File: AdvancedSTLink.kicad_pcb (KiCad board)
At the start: 4 copper layers, 49.9 x 15 mm, 54 parts, among them J1 USB_C_Receptacle, J2 Conn_02x03_Odd_Even, J3 Conn_01x06, J4 Conn_02x03_Odd_Even, SW1 SW_SPDT, U1 STM32F205RETx, U2 XC6206P332MR, U3 USBLC6-2P6, U4 MP2359, U5 USBLC6-2P6, U6 USBLC6-2P6, Y1 X322512MSB4SI

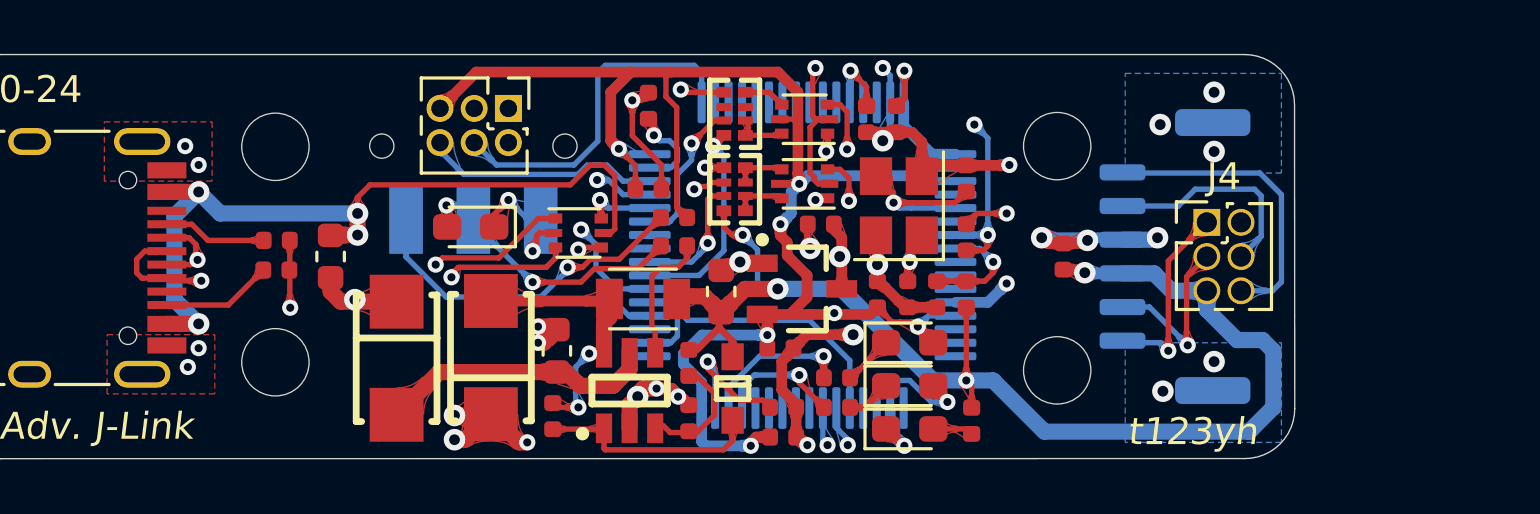
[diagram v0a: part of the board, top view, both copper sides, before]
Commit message: Rearrange RST.
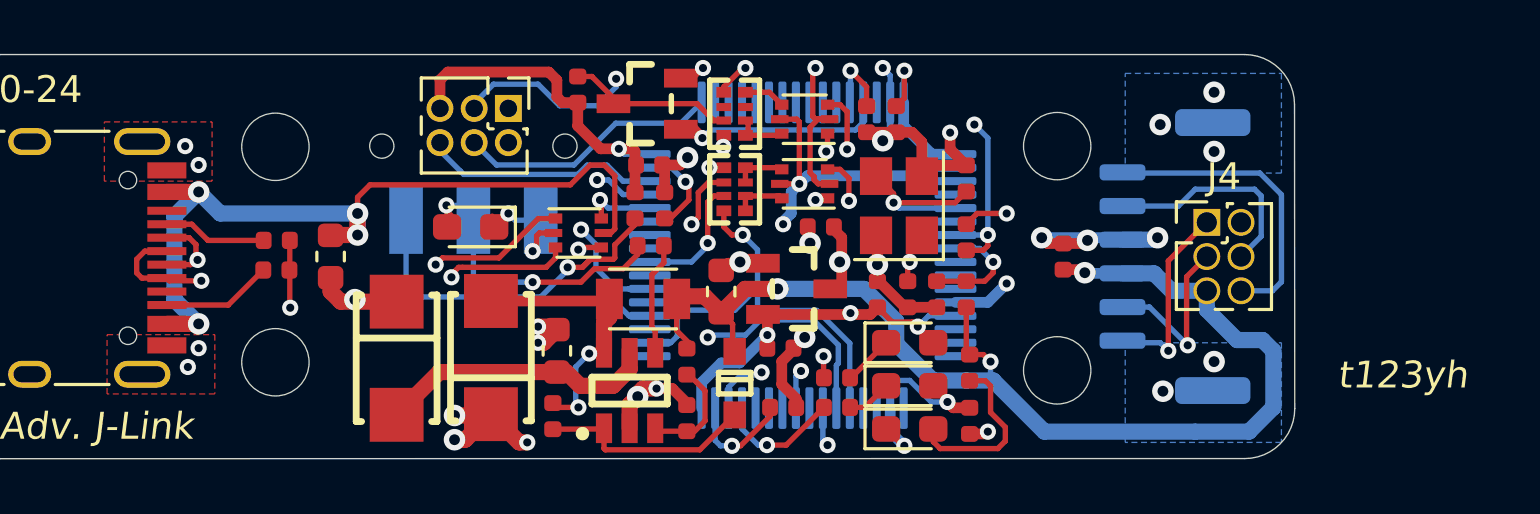
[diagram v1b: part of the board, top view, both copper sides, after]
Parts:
- added Q1: S8050, lc:SOT-23(SOT-23-3), F.Cu at (188.1, 98.8)
- added R6: 10k, Resistor_SMD:R_0402_1005Metric, F.Cu at (185.5, 98.3)
- RN1, RN2: value 220×4 -> 100×4
- U2: footprint lc:SOT-23-3L -> lc:SOT-23(SOT-23-3)
- moved C11 6.95 mm to (200.0, 110.6), turned to 270 degrees
- moved C14 3.75 mm to (188.7, 102.6)
- moved R16 1.98 mm to (200.0, 108.6)
- moved R9 1.52 mm to (187.6, 102.6), turned to 270 degrees
- moved C9 0.90 mm to (188.1, 101.1)
- moved R1 0.87 mm to (188.2, 104.1)
- moved D4 0.21 mm to (191.3, 109.2)
- moved U2 0.20 mm to (193.6, 105.7)
- moved C4 0.10 mm to (194.5, 103.4)
- moved R14 0.09 mm to (189.5, 108.4)
- moved R15 0.07 mm to (189.5, 110.5)
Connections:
- RN2 pad 7: RST2 -> Net-(Q1-Pad3)
- RN2 pad 8: RST1 -> RST_SENSE
- U1 pad 25: Net-(U1-Pad25) -> RST_SENSE
- U1 pad 39: RST1 -> Net-(U1-Pad39)
- U1 pad 61: Net-(U1-Pad61) -> RST_PULL
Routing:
- net RST_SENSE: track 0.00 -> 11.8 mm, vias 0 -> 2
- net +3V3: track 78.6 -> 69.1 mm, vias 9 -> 8
- net RST_PULL: track 0.00 -> 7.89 mm, vias 0 -> 1
- net RST1: track 7.74 -> 0.00 mm, vias 1 -> 0
- net Net-(Q1-Pad3): track 0.00 -> 6.68 mm
- net RST2: track 6.30 -> 0.78 mm, vias 1 -> 0
- net Net-(D5-Pad2): track 1.50 -> 6.63 mm
- net GND: track 65.7 -> 61.1 mm
- net TDO: track 17.8 -> 21.9 mm
- net STM_SWCLK: track 13.0 -> 9.75 mm
- net LED2: track 5.58 -> 7.08 mm, vias 1 -> 2
- net TMS2: track 14.8 -> 15.9 mm
- net Net-(FB1-Pad2): track 29.3 -> 30.1 mm
- net Net-(C14-Pad1): track 3.36 -> 4.16 mm
- net Net-(R1-Pad1): track 4.94 -> 4.21 mm
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
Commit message: 拼板
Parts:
- added C1: 33pF, Capacitor_SMD:C_0402_1005Metric, F.Cu at (176.6, 86.1)
- added C10: 100nF, Capacitor_SMD:C_0402_1005Metric, F.Cu at (177.7, 86.1)
- added C11: 100nF, Capacitor_SMD:C_0402_1005Metric, F.Cu at (174.3, 81.4)
- added C12: 22uF, Capacitor_SMD:C_0603_1608Metric, F.Cu at (183.5, 86.2)
- added C13: 2.2uF, Capacitor_SMD:C_0402_1005Metric, F.Cu at (181.2, 81.9)
- added C14: 2.2uF, Capacitor_SMD:C_0402_1005Metric, F.Cu at (185.6, 89.4)
- added C15: 100nF, Capacitor_SMD:C_0402_1005Metric, F.Cu at (170.8, 87.5)
- added C2: 33pF, Capacitor_SMD:C_0402_1005Metric, F.Cu at (174.4, 90.4)
- added C3: 100nF, Capacitor_SMD:C_0402_1005Metric, F.Cu at (174.4, 88.2)
- added C4: 2.2uF, Capacitor_SMD:C_0402_1005Metric, F.Cu at (179.8, 88.6)
- added C5: 2.2uF, Capacitor_SMD:C_0402_1005Metric, F.Cu at (181.3, 84.1)
- added C6: 10uF, Capacitor_SMD:C_0603_1608Metric, F.Cu at (189.6, 84.0)
- added C7: 100nF, Capacitor_SMD:C_0402_1005Metric, F.Cu at (189.7, 81.6)
- added C8: 100nF, Capacitor_SMD:C_0402_1005Metric, F.Cu at (177.0, 92.6)
- added C9: 100nF, Capacitor_SMD:C_0402_1005Metric, F.Cu at (186.2, 90.9)
- added D1: LED_Red, LED_SMD:LED_0603_1608Metric_Pad1.05x0.95mm_HandSolder, F.Cu at (176.5, 82.7)
- added D2: LED_Yellow, LED_SMD:LED_0603_1608Metric_Pad1.05x0.95mm_HandSolder, F.Cu at (176.5, 84.3)
- added D3: SS34, lc:SMA(DO-214AC)_S1, F.Cu at (192.0, 83.8)
- added D4: 1N4148W, lc:SOD-323, F.Cu at (183.0, 82.8)
- added D5: LED_Blue, LED_SMD:LED_0603_1608Metric_Pad1.05x0.95mm_HandSolder, F.Cu at (176.5, 81.1)
- added D6: LED_Blue, LED_SMD:LED_0603_1608Metric_Pad1.05x0.95mm_HandSolder, F.Cu at (192.8, 88.6)
- added D7: SS34, lc:SMA(DO-214AC)_S1, F.Cu at (195.5, 83.7)
- added FB1: Ferrite_Bead_Small, Inductor_SMD:L_0603_1608Metric, F.Cu at (198.0, 87.5)
- added H1: MountingHole, MountingHole:MountingHole_2.5mm, F.Cu at (171.0, 91.6)
- added H2: MountingHole, MountingHole:MountingHole_2.5mm, F.Cu at (171.0, 83.3)
- added H3: MountingHole, MountingHole:MountingHole_2.5mm, F.Cu at (200.0, 91.6)
- added H4: MountingHole, MountingHole:MountingHole_2.5mm, F.Cu at (200.0, 83.6)
- added J1: USB_C_Receptacle, Connector_USB:USB_C_Receptacle_HRO_TYPE-C-31-M-12, F.Cu at (208.1, 87.5)
- added J2: Conn_02x03_Odd_Even, Connector_PinHeader_1.27mm:PinHeader_2x03_P1.27mm_Vertical, F.Cu at (191.4, 93.0)
- added J3: Conn_01x06, Connector_Molex:Molex_CLIK-Mate_502382-0670_1x06-1MP_P1.25mm_Vertical, B.Cu at (166.6, 87.5)
- added J4: Conn_02x03_Odd_Even, Connector_PinHeader_1.27mm:PinHeader_2x03_P1.27mm_Vertical, F.Cu at (165.4, 88.8)
- added L1: DFE252010P-4R7M, Inductor_SMD:L_TDK_NLV25_2.5x2.0mm, F.Cu at (186.4, 85.9)
- added Q1: S8050, lc:SOT-23(SOT-23-3), F.Cu at (186.2, 93.2)
- added R1: 39k, Resistor_SMD:R_0402_1005Metric, F.Cu at (186.1, 87.9)
- added R14: 120k, Resistor_SMD:R_0402_1005Metric, F.Cu at (184.8, 83.6)
- added R15: 39k, Resistor_SMD:R_0402_1005Metric, F.Cu at (184.8, 81.5)
- added R16: 1.8k, Resistor_SMD:R_0402_1005Metric, F.Cu at (174.3, 83.4)
- added R17: 100k, Resistor_SMD:R_0402_1005Metric, F.Cu at (178.1, 92.6)
- added R2: 10k, Resistor_SMD:R_0402_1005Metric, F.Cu at (175.5, 86.1)
- added R3: 10k, Resistor_SMD:R_0402_1005Metric, F.Cu at (174.4, 86.1)
- added R4: 5.1k, Resistor_SMD:R_0402_1005Metric, F.Cu at (200.0, 88.1)
- added R5: 5.1k, Resistor_SMD:R_0402_1005Metric, F.Cu at (200.0, 87.0)
- added R6: 10k, Resistor_SMD:R_0402_1005Metric, F.Cu at (188.8, 93.7)
- added R7: 2.2k, Resistor_SMD:R_0402_1005Metric, F.Cu at (179.2, 81.9)
- added R8: 2.2k, Resistor_SMD:R_0402_1005Metric, F.Cu at (179.2, 83.0)
- added R9: 2.2k, Resistor_SMD:R_0402_1005Metric, F.Cu at (186.7, 89.4)
- added RN1: 100×4, lc:0402_RX4, F.Cu at (183.0, 90.0)
- added RN2: 100×4, lc:0402_RX4, F.Cu at (183.0, 92.8)
- added SW1: SW_SPDT, Button_Switch_SMD:SW_SPDT_CK-JS102011SAQN, B.Cu at (192.7, 91.6)
- added U1: STM32F205RETx, Package_QFP:LQFP-64_10x10mm_P0.5mm, B.Cu at (180.5, 87.5)
- added U2: XC6206P332MR, lc:SOT-23(SOT-23-3), F.Cu at (180.7, 86.3)
- added U3: USBLC6-2P6, Package_TO_SOT_SMD:SOT-666, F.Cu at (188.8, 88.4)
- added U4: MP2359, lc:SOT-23-6, F.Cu at (186.9, 82.5)
- added U5: USBLC6-2P6, Package_TO_SOT_SMD:SOT-666, F.Cu at (180.4, 92.6)
- added U6: USBLC6-2P6, Package_TO_SOT_SMD:SOT-666, F.Cu at (180.4, 90.2)
- added Y1: X322512MSB4SI, Crystal:Crystal_SMD_3225-4Pin_3.2x2.5mm, F.Cu at (176.9, 89.4)
- added mouse-bite-3mm-slot: VAL**, mouse_bite:mouse-bite-3mm-slot, F.Cu at (170.0, 96.0)
- added mouse-bite-3mm-slot: VAL**, mouse_bite:mouse-bite-3mm-slot, F.Cu at (204.3, 96.0)
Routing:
- net (no net): track 0.00 -> 665.8 mm, vias 0 -> 94
- added copper zone on B.Cu, net (none)
- added copper zone on F.Cu, net (none)
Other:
- board size 49.9 x 15 mm -> 49.9 x 32 mm

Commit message: fabrication version
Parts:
- FB1 (x2): footprint Inductor_SMD:L_0603_1608Metric -> Inductor_SMD:L_0805_2012Metric
- moved FB1 1.95 mm to (196.2, 88.4), turned to 0 degrees
- moved FB1 1.95 mm to (178.0, 103.6), turned to 180 degrees
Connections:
- C1 pad 1: (no net) -> Net-(C1-Pad1)
- C1 pad 2: (no net) -> GND
- C10 pad 1: (no net) -> +3V3
- C10 pad 2: (no net) -> GND
- C11 pad 1: (no net) -> +3V3
- C11 pad 2: (no net) -> GND
- C12 pad 1: (no net) -> V_OUT_3.3
- C12 pad 2: (no net) -> GND
- C13 pad 1: (no net) -> GND
- C13 pad 2: (no net) -> Net-(C13-Pad2)
- C14 pad 1: (no net) -> Net-(C14-Pad1)
- C14 pad 2: (no net) -> GND
- C15 pad 1: (no net) -> V_OUT_3.3
- C15 pad 2: (no net) -> GND
- C2 pad 1: (no net) -> GND
- C2 pad 2: (no net) -> Net-(C2-Pad2)
- C3 pad 1: (no net) -> GND
- C3 pad 2: (no net) -> STM_NRST
- C4 pad 1: (no net) -> VBUS
- C4 pad 2: (no net) -> GND
- C5 pad 1: (no net) -> +3V3
- C5 pad 2: (no net) -> GND
- C6 pad 1: (no net) -> Net-(C6-Pad1)
- C6 pad 2: (no net) -> GND
- C7 pad 1: (no net) -> Net-(C7-Pad1)
- C7 pad 2: (no net) -> Net-(C7-Pad2)
- C8 pad 1: (no net) -> +3V3
- C8 pad 2: (no net) -> GND
- C9 pad 1: (no net) -> +3V3
- C9 pad 2: (no net) -> GND
- D1 pad 1: (no net) -> Net-(D1-Pad1)
- D1 pad 2: (no net) -> +3V3
- D2 pad 1: (no net) -> Net-(D2-Pad1)
- D2 pad 2: (no net) -> +3V3
- D3 pad 1: (no net) -> Net-(C7-Pad2)
- D3 pad 2: (no net) -> GND
- D4 pad 1: (no net) -> Net-(C7-Pad1)
- D4 pad 2: (no net) -> V_OUT_3.3
- D5 pad 1: (no net) -> GND
- D5 pad 2: (no net) -> Net-(D5-Pad2)
- D6 pad 1: (no net) -> GND
- D6 pad 2: (no net) -> Net-(D6-Pad2)
- D7 pad 1: (no net) -> Net-(C6-Pad1)
- D7 pad 2: (no net) -> VBUS
- FB1 pad 1: (no net) -> VBUS
- FB1 pad 2: (no net) -> Net-(FB1-Pad2)
- J1 pad A1: (no net) -> GND
- J1 pad A12: (no net) -> GND
- J1 pad A4: (no net) -> Net-(FB1-Pad2)
- J1 pad A5: (no net) -> Net-(J1-PadA5)
- J1 pad A6: (no net) -> USB_IN_DP
- J1 pad A7: (no net) -> USB_IN_DN
- J1 pad A8: (no net) -> Net-(J1-PadA8)
- J1 pad A9: (no net) -> Net-(FB1-Pad2)
- J1 pad B1: (no net) -> GND
- J1 pad B12: (no net) -> GND
- J1 pad B4: (no net) -> Net-(FB1-Pad2)
- J1 pad B5: (no net) -> Net-(J1-PadB5)
- J1 pad B6: (no net) -> USB_IN_DP
- J1 pad B7: (no net) -> USB_IN_DN
- J1 pad B8: (no net) -> Net-(J1-PadB8)
- J1 pad B9: (no net) -> Net-(FB1-Pad2)
- J1 pad S1: (no net) -> GND
- J2 pad 1: (no net) -> Net-(J2-Pad1)
- J2 pad 2: (no net) -> GND
- J2 pad 3: (no net) -> STM_NRST
- J2 pad 4: (no net) -> STM_SWCLK
- J2 pad 5: (no net) -> +3V3
- J2 pad 6: (no net) -> STM_SWDIO
- J3 pad 1: (no net) -> T_SWO_O
- J3 pad 2: (no net) -> T_NRST_O
- J3 pad 3: (no net) -> V_OUT_3.3
- J3 pad 4: (no net) -> GND
- J3 pad 5: (no net) -> T_SWCLK_O
- J3 pad 6: (no net) -> T_SWDIO_O
- J3 pad MP: (no net) -> GND
- J4 pad 1: (no net) -> T_SWO_O
- J4 pad 2: (no net) -> GND
- J4 pad 3: (no net) -> T_NRST_O
- J4 pad 4: (no net) -> T_SWCLK_O
- J4 pad 5: (no net) -> V_OUT_3.3
- J4 pad 6: (no net) -> T_SWDIO_O
- L1 pad 1: (no net) -> Net-(C7-Pad2)
- L1 pad 2: (no net) -> V_OUT_3.3
- Q1 pad 1: (no net) -> RST_PULL
- Q1 pad 2: (no net) -> GND
- Q1 pad 3: (no net) -> Net-(Q1-Pad3)
- R1 pad 1: (no net) -> Net-(R1-Pad1)
- R1 pad 2: (no net) -> Net-(D6-Pad2)
- R14 pad 1: (no net) -> Net-(R14-Pad1)
- R14 pad 2: (no net) -> V_OUT_3.3
- R15 pad 1: (no net) -> GND
- R15 pad 2: (no net) -> Net-(R14-Pad1)
- R16 pad 1: (no net) -> Net-(D5-Pad2)
- R16 pad 2: (no net) -> V_OUT_3.3
- R17 pad 1: (no net) -> Net-(R17-Pad1)
- R17 pad 2: (no net) -> GND
- R2 pad 1: (no net) -> GND
- R2 pad 2: (no net) -> Net-(R2-Pad2)
- R3 pad 1: (no net) -> V_OUT_3.3
- R3 pad 2: (no net) -> Net-(R2-Pad2)
- R4 pad 1: (no net) -> GND
- R4 pad 2: (no net) -> Net-(J1-PadA5)
- R5 pad 1: (no net) -> GND
- R5 pad 2: (no net) -> Net-(J1-PadB5)
- R6 pad 1: (no net) -> Net-(Q1-Pad3)
- R6 pad 2: (no net) -> +3V3
- R7 pad 1: (no net) -> Net-(D1-Pad1)
- R7 pad 2: (no net) -> LED1
- R8 pad 1: (no net) -> Net-(D2-Pad1)
- R8 pad 2: (no net) -> LED2
- R9 pad 1: (no net) -> +3V3
- R9 pad 2: (no net) -> Net-(R9-Pad2)
- RN1 pad 1: (no net) -> T_SWCLK_I
- RN1 pad 2: (no net) -> T_SWCLK_I
- RN1 pad 3: (no net) -> T_SWDIO_I
- RN1 pad 4: (no net) -> T_SWDIO_I
- RN1 pad 5: (no net) -> TMS1
- RN1 pad 6: (no net) -> TMS2
- RN1 pad 7: (no net) -> TCK2
- RN1 pad 8: (no net) -> TCK1
- RN2 pad 1: (no net) -> T_NRST_I
- RN2 pad 2: (no net) -> T_NRST_I
- RN2 pad 3: (no net) -> Net-(RN2-Pad3)
- RN2 pad 4: (no net) -> T_SWO_I
- RN2 pad 5: (no net) -> TDO
- RN2 pad 6: (no net) -> Net-(RN2-Pad6)
- RN2 pad 7: (no net) -> Net-(Q1-Pad3)
- RN2 pad 8: (no net) -> RST_SENSE
- SW1 pad 1: (no net) -> Net-(R9-Pad2)
- SW1 pad 2: (no net) -> Net-(D6-Pad2)
- SW1 pad 3: (no net) -> GND
- U1 pad 1: (no net) -> +3V3
- U1 pad 10: (no net) -> Net-(U1-Pad10)
- U1 pad 11: (no net) -> Net-(U1-Pad11)
- U1 pad 12: (no net) -> GND
- U1 pad 13: (no net) -> +3V3
- U1 pad 14: (no net) -> Net-(U1-Pad14)
- U1 pad 15: (no net) -> Net-(U1-Pad15)
- U1 pad 16: (no net) -> Net-(U1-Pad16)
- U1 pad 17: (no net) -> Net-(U1-Pad17)
- U1 pad 18: (no net) -> GND
- U1 pad 19: (no net) -> +3V3
- U1 pad 2: (no net) -> Net-(U1-Pad2)
- U1 pad 20: (no net) -> Net-(U1-Pad20)
- U1 pad 21: (no net) -> TCK1
- U1 pad 22: (no net) -> TMS1
- U1 pad 23: (no net) -> TMS2
- U1 pad 24: (no net) -> Net-(U1-Pad24)
- U1 pad 25: (no net) -> RST_SENSE
- U1 pad 26: (no net) -> Net-(U1-Pad26)
- U1 pad 27: (no net) -> Net-(U1-Pad27)
- U1 pad 28: (no net) -> Net-(U1-Pad28)
- U1 pad 29: (no net) -> LED1
- U1 pad 3: (no net) -> Net-(U1-Pad3)
- U1 pad 30: (no net) -> LED2
- U1 pad 31: (no net) -> Net-(C13-Pad2)
- U1 pad 32: (no net) -> +3V3
- U1 pad 33: (no net) -> Net-(U1-Pad33)
- U1 pad 34: (no net) -> TCK1
- U1 pad 35: (no net) -> Net-(U1-Pad35)
- U1 pad 36: (no net) -> TDO
- U1 pad 37: (no net) -> TCK1
- U1 pad 38: (no net) -> TDO
- U1 pad 39: (no net) -> Net-(U1-Pad39)
- U1 pad 4: (no net) -> Net-(U1-Pad4)
- U1 pad 40: (no net) -> TCK2
- U1 pad 41: (no net) -> Net-(U1-Pad41)
- U1 pad 42: (no net) -> Net-(U1-Pad42)
- U1 pad 43: (no net) -> RST2
- U1 pad 44: (no net) -> USB_DN
- U1 pad 45: (no net) -> USB_DP
- U1 pad 46: (no net) -> STM_SWDIO
- U1 pad 47: (no net) -> Net-(C14-Pad1)
- U1 pad 48: (no net) -> +3V3
- U1 pad 49: (no net) -> STM_SWCLK
- U1 pad 5: (no net) -> Net-(C2-Pad2)
- U1 pad 50: (no net) -> Net-(U1-Pad50)
- U1 pad 51: (no net) -> Net-(U1-Pad51)
- U1 pad 52: (no net) -> Net-(U1-Pad52)
- U1 pad 53: (no net) -> Net-(U1-Pad53)
- U1 pad 54: (no net) -> Net-(U1-Pad54)
- U1 pad 55: (no net) -> Net-(U1-Pad55)
- U1 pad 56: (no net) -> Net-(U1-Pad56)
- U1 pad 57: (no net) -> Net-(U1-Pad57)
- U1 pad 58: (no net) -> Net-(U1-Pad58)
- U1 pad 59: (no net) -> Net-(U1-Pad59)
- U1 pad 6: (no net) -> Net-(C1-Pad1)
- U1 pad 60: (no net) -> Net-(R17-Pad1)
- U1 pad 61: (no net) -> RST_PULL
- U1 pad 62: (no net) -> Net-(U1-Pad62)
- U1 pad 63: (no net) -> GND
- U1 pad 64: (no net) -> +3V3
- U1 pad 7: (no net) -> STM_NRST
- U1 pad 8: (no net) -> Net-(R2-Pad2)
- U1 pad 9: (no net) -> Net-(U1-Pad9)
- U2 pad 1: (no net) -> GND
- U2 pad 2: (no net) -> +3V3
- U2 pad 3: (no net) -> VBUS
- U3 pad 1: (no net) -> USB_IN_DN
- U3 pad 2: (no net) -> GND
- U3 pad 3: (no net) -> USB_IN_DP
- U3 pad 4: (no net) -> USB_DP
- U3 pad 5: (no net) -> Net-(FB1-Pad2)
- U3 pad 6: (no net) -> USB_DN
- U4 pad 1: (no net) -> Net-(C7-Pad1)
- U4 pad 2: (no net) -> GND
- U4 pad 3: (no net) -> Net-(R14-Pad1)
- U4 pad 4: (no net) -> Net-(R1-Pad1)
- U4 pad 5: (no net) -> Net-(C6-Pad1)
- U4 pad 6: (no net) -> Net-(C7-Pad2)
- U5 pad 1: (no net) -> T_NRST_O
- U5 pad 2: (no net) -> GND
- U5 pad 3: (no net) -> T_SWO_O
- U5 pad 4: (no net) -> T_SWO_I
- U5 pad 5: (no net) -> +3V3
- U5 pad 6: (no net) -> T_NRST_I
- U6 pad 1: (no net) -> T_SWCLK_O
- U6 pad 2: (no net) -> GND
- U6 pad 3: (no net) -> T_SWDIO_O
- U6 pad 4: (no net) -> T_SWDIO_I
- U6 pad 5: (no net) -> +3V3
- U6 pad 6: (no net) -> T_SWCLK_I
- Y1 pad 1: (no net) -> Net-(C1-Pad1)
- Y1 pad 2: (no net) -> GND
- Y1 pad 3: (no net) -> Net-(C2-Pad2)
- Y1 pad 4: (no net) -> GND
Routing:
- net (no net): track 665.8 -> 0.00 mm, vias 94 -> 0
- net +3V3: track 69.1 -> 138.1 mm, vias 8 -> 16
- net GND: track 61.1 -> 122.3 mm, vias 36 -> 72
- net V_OUT_3.3: track 44.7 -> 89.4 mm, vias 3 -> 6
- net Net-(FB1-Pad2): track 30.1 -> 63.7 mm, vias 4 -> 8
- net VBUS: track 31.0 -> 64.2 mm, vias 2 -> 4
- net T_SWCLK_O: track 29.7 -> 59.5 mm, vias 1 -> 2
- net T_SWDIO_O: track 29.5 -> 59.0 mm, vias 1 -> 2
- net STM_NRST: track 27.9 -> 55.7 mm, vias 3 -> 6
- net T_NRST_O: track 24.9 -> 49.9 mm, vias 2 -> 4
- net T_SWO_O: track 23.9 -> 47.8 mm, vias 2 -> 4
- net TDO: track 21.9 -> 43.9 mm, vias 2 -> 4
- net USB_IN_DP: track 18.3 -> 36.5 mm, vias 2 -> 4
- net TCK1: track 17.4 -> 34.8 mm, vias 1 -> 2
- net USB_IN_DN: track 17.0 -> 34.1 mm, vias 2 -> 4
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- removed copper zone on B.Cu, net (none)
- removed copper zone on F.Cu, net (none)
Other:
- outline, holes or cut-outs redrawn
